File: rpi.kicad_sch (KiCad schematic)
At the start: 1 part, among them J1 Raspberry_Pi_2_3

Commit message: more schematic
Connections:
- net RO: now reaches J1.10 (GPIO15/RXD)
- net RST: now reaches J1.11 (GPIO17)
- net BI: now reaches J1.36 (GPIO16)
- net CI: now reaches J1.8 (GPIO14/TXD)
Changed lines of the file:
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@@
+    (stroke (width 0) (type default))
+  )
+  (wire (pts (xy 64.135 59.055) (xy 68.58 59.055))
     (stroke (width 0) (type default))
   )
@@
     (stroke (width 0) (type default))
   )
+  (wire (pts (xy 64.135 51.435) (xy 68.58 51.435))
+    (stroke (width 0) (type default))
+  )
+  (wire (pts (xy 64.135 48.895) (xy 68.58 48.895))
+    (stroke (width 0) (type default))
+  )
   (wire (pts (xy 86.36 104.775) (xy 86.36 106.68))
     (stroke (width 0) (type default))
@@
     (stroke (width 0) (type default))
   )
+  (wire (pts (xy 64.135 56.515) (xy 68.58 56.515))
+    (stroke (width 0) (type default))
+  )
   (global_label "GND" (shape input) (at 87.63 111.76 0) (fields_autoplaced)
     (effects (font (size 1.27 1.27)) (justify left))
@@
     (effects (font (size 1.27 1.27)) (justify left))
   )
+  (hierarchical_label "RO" (shape input) (at 64.135 51.435 180) (fields_autoplaced)
+    (effects (font (size 1.27 1.27)) (justify right))
+  )
+  (hierarchical_label "BI" (shape output) (at 64.135 56.515 180) (fields_autoplaced)
+    (effects (font (size 1.27 1.27)) (justify right))
+  )
+  (hierarchical_label "RST" (shape output) (at 64.135 59.055 180) (fields_autoplaced)
+    (effects (font (size 1.27 1.27)) (justify right))
+  )
+  (hierarchical_label "CI" (shape output) (at 64.135 48.895 180) (fields_autoplaced)
+    (effects (font (size 1.27 1.27)) (justify right))
+  )
   (hierarchical_label "5V" (shape input) (at 85.09 31.75 90) (fields_autoplaced)

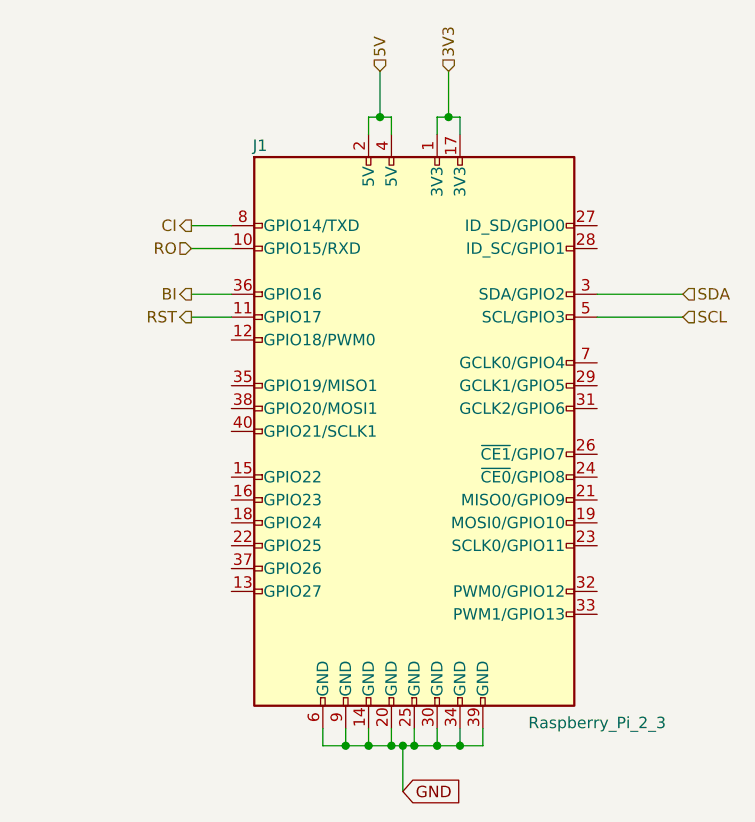
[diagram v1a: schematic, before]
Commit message: cleanup level shifters. LCRC inductor for buck
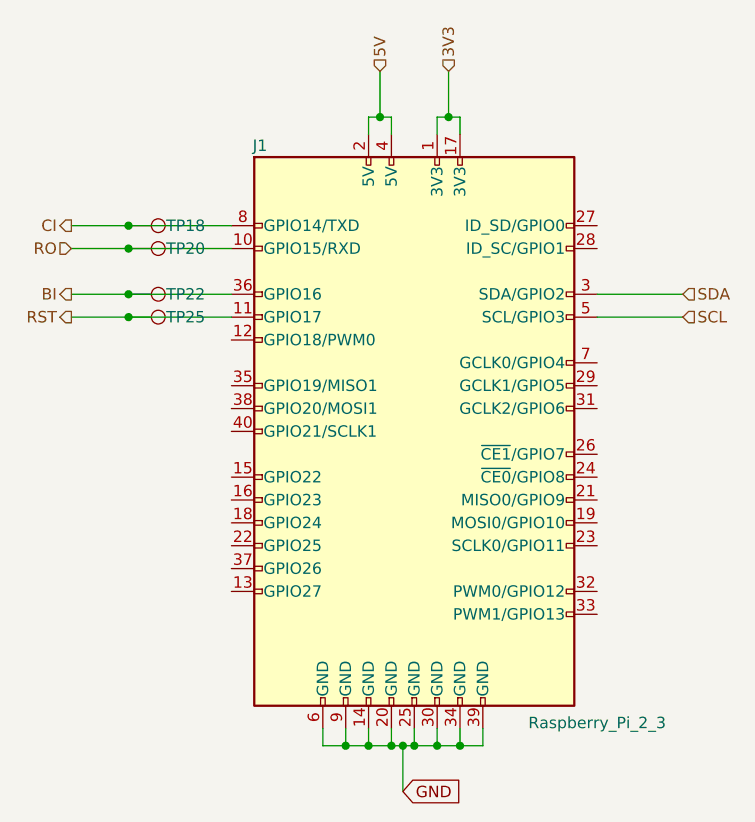
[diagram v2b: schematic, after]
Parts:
- added TP18, TP20, TP22, TP25: TestPoint, TestPoint:TestPoint_Pad_D1.5mm, symbol Connector:TestPoint
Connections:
- net BI: now also TP22.1
- net CI: now also TP18.1
- net RO: now also TP20.1
- net RST: now also TP25.1
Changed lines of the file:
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@@
   (junction (at 92.71 36.83) (diameter 0) (color 0 0 0 0)
   )
+  (junction (at 57.15 59.055) (diameter 0) (color 0 0 0 0)
+  )
+  (junction (at 57.15 51.435) (diameter 0) (color 0 0 0 0)
+  )
+  (junction (at 57.15 56.515) (diameter 0) (color 0 0 0 0)
+  )
   (junction (at 91.44 106.68) (diameter 0) (color 0 0 0 0)
   )
@@
   (junction (at 81.28 106.68) (diameter 0) (color 0 0 0 0)
   )
+  (junction (at 57.15 48.895) (diameter 0) (color 0 0 0 0)
+  )
   (junction (at 88.9 106.68) (diameter 0) (color 0 0 0 0)
   )
@@
     (stroke (width 0) (type default))
   )
-  (wire (pts (xy 64.135 59.055) (xy 68.58 59.055))
+  (wire (pts (xy 50.8 59.055) (xy 57.15 59.055))
     (stroke (width 0) (type default))
   )
@@
     (stroke (width 0) (type default))
   )
+  (wire (pts (xy 57.15 51.435) (xy 68.58 51.435))
+    (stroke (width 0) (type default))
+  )
   (wire (pts (xy 78.74 106.68) (xy 81.28 106.68))
     (stroke (width 0) (type default))
   )
+  (wire (pts (xy 57.15 56.515) (xy 68.58 56.515))
+    (stroke (width 0) (type default))
+  )
   (wire (pts (xy 83.82 36.83) (xy 85.09 36.83))
     (stroke (width 0) (type default))
@@
     (stroke (width 0) (type default))
   )
-  (wire (pts (xy 64.135 51.435) (xy 68.58 51.435))
-    (stroke (width 0) (type default))
-  )
-  (wire (pts (xy 64.135 48.895) (xy 68.58 48.895))
+  (wire (pts (xy 50.8 51.435) (xy 57.15 51.435))
+    (stroke (width 0) (type default))
+  )
+  (wire (pts (xy 50.8 48.895) (xy 57.15 48.895))
     (stroke (width 0) (type default))
   )
@@
     (stroke (width 0) (type default))
   )
+  (wire (pts (xy 57.15 59.055) (xy 68.58 59.055))
+    (stroke (width 0) (type default))
+  )
+  (wire (pts (xy 57.15 48.895) (xy 68.58 48.895))
+    (stroke (width 0) (type default))
+  )
   (wire (pts (xy 81.28 106.68) (xy 83.82 106.68))
     (stroke (width 0) (type default))
@@
     (stroke (width 0) (type default))
   )
-  (wire (pts (xy 64.135 56.515) (xy 68.58 56.515))
+  (wire (pts (xy 50.8 56.515) (xy 57.15 56.515))
     (stroke (width 0) (type default))
   )
@@
     (effects (font (size 1.27 1.27)) (justify left))
   )
-  (hierarchical_label "RO" (shape input) (at 64.135 51.435 180) (fields_autoplaced)
+  (hierarchical_label "RO" (shape input) (at 50.8 51.435 180) (fields_autoplaced)
     (effects (font (size 1.27 1.27)) (justify right))
   )
-  (hierarchical_label "BI" (shape output) (at 64.135 56.515 180) (fields_autoplaced)
+  (hierarchical_label "BI" (shape output) (at 50.8 56.515 180) (fields_autoplaced)
     (effects (font (size 1.27 1.27)) (justify right))
   )
-  (hierarchical_label "RST" (shape output) (at 64.135 59.055 180) (fields_autoplaced)
+  (hierarchical_label "RST" (shape output) (at 50.8 59.055 180) (fields_autoplaced)
     (effects (font (size 1.27 1.27)) (justify right))
   )
-  (hierarchical_label "CI" (shape output) (at 64.135 48.895 180) (fields_autoplaced)
+  (hierarchical_label "CI" (shape output) (at 50.8 48.895 180) (fields_autoplaced)
     (effects (font (size 1.27 1.27)) (justify right))
   )
@@
   (hierarchical_label "SDA" (shape input) (at 118.745 56.515 0) (fields_autoplaced)
     (effects (font (size 1.27 1.27)) (justify left))
+  )
+  (symbol (lib_id "Connector:TestPoint") (at 57.15 51.435 270) (mirror x) (unit 1)
+    (in_bom yes) (on_board yes) (dnp no)
+    (property "Reference" "TP20" (at 63.5 51.435 90)
+      (effects (font (size 1.27 1.27)))
+    )
+    (property "Value" "TestPoint" (at 62.865 50.1651 90)
+      (effects (font (size 1.27 1.27)) (justify left) hide)
+    )
+    (property "Footprint" "TestPoint:TestPoint_Pad_D1.5mm" (at 57.15 46.355 0)
+      (effects (font (size 1.27 1.27)) hide)
+    )
+    (property "Datasheet" "~" (at 57.15 46.355 0)
+      (effects (font (size 1.27 1.27)) hide)
+    )
+    (property "DNP" "T" (at 57.15 51.435 0)
+      (effects (font (size 1.27 1.27)) hide)
+    )
+    (pin "1")
+    (instances
+      (project "Hashat"
+        (path "/00740941-7ad8-466a-a267-188591e2b5c4/5aa25910-cf6c-433c-86f8-40d28be84b47"
+          (reference "TP20") (unit 1)
+        )
+        (path "/00740941-7ad8-466a-a267-188591e2b5c4/17c7154e-4e6a-44f7-b397-e76bf5123af9"
+          (reference "TP20") (unit 1)
+        )
+      )
+      (project "bitaxeMax"
+        (path "/e63e39d7-6ac0-4ffd-8aa3-1841a4541b55/4cf9c075-d009-4c35-9949-adda70ae20c7"
+          (reference "TP24") (unit 1)
+        )
+      )
+    )
+  )
+  (symbol (lib_id "Connector:TestPoint") (at 57.15 48.895 270) (mirror x) (unit 1)
+    (in_bom yes) (on_board yes) (dnp no)
+    (property "Reference" "TP18" (at 63.5 48.895 90)
+      (effects (font (size 1.27 1.27)))
+    )
+    (property "Value" "TestPoint" (at 62.865 47.6251 90)
+      (effects (font (size 1.27 1.27)) (justify left) hide)
+    )
+    (property "Footprint" "TestPoint:TestPoint_Pad_D1.5mm" (at 57.15 43.815 0)
+      (effects (font (size 1.27 1.27)) hide)
+    )
+    (property "Datasheet" "~" (at 57.15 43.815 0)
+      (effects (font (size 1.27 1.27)) hide)
+    )
+    (property "DNP" "T" (at 57.15 48.895 0)
+      (effects (font (size 1.27 1.27)) hide)
+    )
+    (pin "1")
+    (instances
+      (project "Hashat"
+        (path "/00740941-7ad8-466a-a267-188591e2b5c4/5aa25910-cf6c-433c-86f8-40d28be84b47"
+          (reference "TP18") (unit 1)
+        )
+        (path "/00740941-7ad8-466a-a267-188591e2b5c4/17c7154e-4e6a-44f7-b397-e76bf5123af9"
+          (reference "TP18") (unit 1)
+        )
+      )
+      (project "bitaxeMax"
+        (path "/e63e39d7-6ac0-4ffd-8aa3-1841a4541b55/4cf9c075-d009-4c35-9949-adda70ae20c7"
+          (reference "TP24") (unit 1)
+        )
+      )
+    )
   )
   (symbol (lib_id "Connector:Raspberry_Pi_2_3") (at 88.9 71.755 0) (unit 1)
@@
         )
       )
+    )
+  )
+  (symbol (lib_id "Connector:TestPoint") (at 57.15 56.515 270) (mirror x) (unit 1)
+    (in_bom yes) (on_board yes) (dnp no)
+    (property "Reference" "TP22" (at 63.5 56.515 90)
+      (effects (font (size 1.27 1.27)))
+    )
+    (property "Value" "TestPoint" (at 62.865 55.2451 90)
+      (effects (font (size 1.27 1.27)) (justify left) hide)
+    )
+    (property "Footprint" "TestPoint:TestPoint_Pad_D1.5mm" (at 57.15 51.435 0)
+      (effects (font (size 1.27 1.27)) hide)
+    )
+    (property "Datasheet" "~" (at 57.15 51.435 0)
+      (effects (font (size 1.27 1.27)) hide)
+    )
+    (property "DNP" "T" (at 57.15 56.515 0)
+      (effects (font (size 1.27 1.27)) hide)
+    )
+    (pin "1")
+    (instances
+      (project "Hashat"
+        (path "/00740941-7ad8-466a-a267-188591e2b5c4/5aa25910-cf6c-433c-86f8-40d28be84b47"
+          (reference "TP22") (unit 1)
+        )
+        (path "/00740941-7ad8-466a-a267-188591e2b5c4/17c7154e-4e6a-44f7-b397-e76bf5123af9"
+          (reference "TP22") (unit 1)
+        )
+      )
+      (project "bitaxeMax"
+        (path "/e63e39d7-6ac0-4ffd-8aa3-1841a4541b55/4cf9c075-d009-4c35-9949-adda70ae20c7"
+          (reference "TP24") (unit 1)
+        )
+      )
+    )
+  )
+  (symbol (lib_id "Connector:TestPoint") (at 57.15 59.055 270) (mirror x) (unit 1)
+    (in_bom yes) (on_board yes) (dnp no)
+    (property "Reference" "TP25" (at 63.5 59.055 90)
+      (effects (font (size 1.27 1.27)))
+    )
+    (property "Value" "TestPoint" (at 62.865 57.7851 90)
+      (effects (font (size 1.27 1.27)) (justify left) hide)
+    )
+    (property "Footprint" "TestPoint:TestPoint_Pad_D1.5mm" (at 57.15 53.975 0)
+      (effects (font (size 1.27 1.27)) hide)
+    )
+    (property "Datasheet" "~" (at 57.15 53.975 0)
+      (effects (font (size 1.27 1.27)) hide)
+    )
+    (property "DNP" "T" (at 57.15 59.055 0)
+      (effects (font (size 1.27 1.27)) hide)
+    )
+    (pin "1")
+    (instances
+      (project "Hashat"
+        (path "/00740941-7ad8-466a-a267-188591e2b5c4/5aa25910-cf6c-433c-86f8-40d28be84b47"
+          (reference "TP25") (unit 1)
+        )
+        (path "/00740941-7ad8-466a-a267-188591e2b5c4/17c7154e-4e6a-44f7-b397-e76bf5123af9"
+          (reference "TP25") (unit 1)
+        )
+      )
+      (project "bitaxeMax"
+        (path "/e63e39d7-6ac0-4ffd-8aa3-1841a4541b55/4cf9c075-d009-4c35-9949-adda70ae20c7"
+          (reference "TP24") (unit 1)
+        )
+      )

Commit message: fully removed BI (and pulled down at the BM1397)
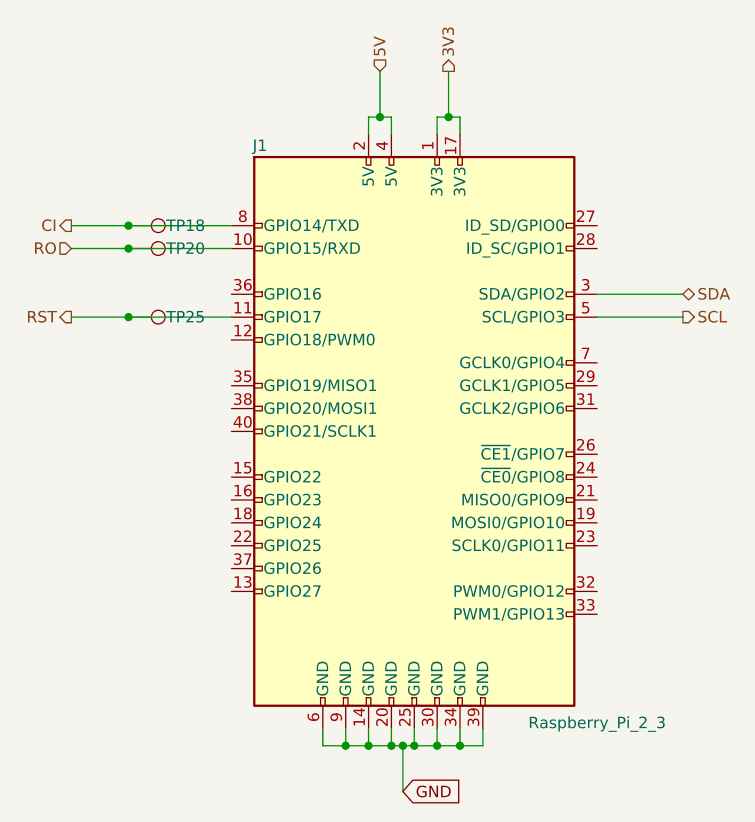
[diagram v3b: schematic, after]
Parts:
- removed TP22: TestPoint, TestPoint:TestPoint_Pad_D1.5mm, symbol Connector:TestPoint
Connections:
- net BI: no longer names the net of J1.36 (GPIO16)
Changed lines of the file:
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@@
   (junction (at 57.15 51.435) (diameter 0) (color 0 0 0 0)
   )
-  (junction (at 57.15 56.515) (diameter 0) (color 0 0 0 0)
-  )
   (junction (at 91.44 106.68) (diameter 0) (color 0 0 0 0)
   )
@@
     (stroke (width 0) (type default))
   )
-  (wire (pts (xy 57.15 56.515) (xy 68.58 56.515))
-    (stroke (width 0) (type default))
-  )
   (wire (pts (xy 83.82 36.83) (xy 85.09 36.83))
     (stroke (width 0) (type default))
@@
   )
   (wire (pts (xy 83.82 106.68) (xy 86.36 106.68))
-    (stroke (width 0) (type default))
-  )
-  (wire (pts (xy 50.8 56.515) (xy 57.15 56.515))
     (stroke (width 0) (type default))
   )
@@
     )
   )
-  (hierarchical_label "3V3" (shape input) (at 92.71 31.75 90) (fields_autoplaced)
+  (hierarchical_label "3V3" (shape output) (at 92.71 31.75 90) (fields_autoplaced)
     (effects (font (size 1.27 1.27)) (justify left))
   )
@@
     (effects (font (size 1.27 1.27)) (justify right))
   )
-  (hierarchical_label "BI" (shape output) (at 50.8 56.515 180) (fields_autoplaced)
-    (effects (font (size 1.27 1.27)) (justify right))
-  )
   (hierarchical_label "RST" (shape output) (at 50.8 59.055 180) (fields_autoplaced)
     (effects (font (size 1.27 1.27)) (justify right))
@@
     (effects (font (size 1.27 1.27)) (justify left))
   )
-  (hierarchical_label "SCL" (shape input) (at 118.745 59.055 0) (fields_autoplaced)
-    (effects (font (size 1.27 1.27)) (justify left))
-  )
-  (hierarchical_label "SDA" (shape input) (at 118.745 56.515 0) (fields_autoplaced)
+  (hierarchical_label "SCL" (shape output) (at 118.745 59.055 0) (fields_autoplaced)
+    (effects (font (size 1.27 1.27)) (justify left))
+  )
+  (hierarchical_label "SDA" (shape bidirectional) (at 118.745 56.515 0) (fields_autoplaced)
     (effects (font (size 1.27 1.27)) (justify left))
   )
@@
         )
       )
-    )
-  )
-  (symbol (lib_id "Connector:TestPoint") (at 57.15 56.515 270) (mirror x) (unit 1)
-    (in_bom yes) (on_board yes) (dnp no)
-    (property "Reference" "TP22" (at 63.5 56.515 90)
-      (effects (font (size 1.27 1.27)))
-    )
-    (property "Value" "TestPoint" (at 62.865 55.2451 90)
-      (effects (font (size 1.27 1.27)) (justify left) hide)
-    )
-    (property "Footprint" "TestPoint:TestPoint_Pad_D1.5mm" (at 57.15 51.435 0)
-      (effects (font (size 1.27 1.27)) hide)
-    )
-    (property "Datasheet" "~" (at 57.15 51.435 0)
-      (effects (font (size 1.27 1.27)) hide)
-    )
-    (property "DNP" "T" (at 57.15 56.515 0)
-      (effects (font (size 1.27 1.27)) hide)
-    )
-    (pin "1")
-    (instances
-      (project "Hashat"
-        (path "/00740941-7ad8-466a-a267-188591e2b5c4/5aa25910-cf6c-433c-86f8-40d28be84b47"
-          (reference "TP22") (unit 1)
-        )
-        (path "/00740941-7ad8-466a-a267-188591e2b5c4/17c7154e-4e6a-44f7-b397-e76bf5123af9"
-          (reference "TP22") (unit 1)
-        )
-      )
-      (project "bitaxeMax"
-        (path "/e63e39d7-6ac0-4ffd-8aa3-1841a4541b55/4cf9c075-d009-4c35-9949-adda70ae20c7"
-          (reference "TP24") (unit 1)
-        )
-      )

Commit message: added initial BOM
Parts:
- TP18, TP20, TP25: now left out of the parts list
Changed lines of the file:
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@@
   )
   (symbol (lib_id "Connector:TestPoint") (at 57.15 51.435 270) (mirror x) (unit 1)
-    (in_bom yes) (on_board yes) (dnp no)
+    (in_bom no) (on_board yes) (dnp no)
     (property "Reference" "TP20" (at 63.5 51.435 90)
       (effects (font (size 1.27 1.27)))
@@
   )
   (symbol (lib_id "Connector:TestPoint") (at 57.15 48.895 270) (mirror x) (unit 1)
-    (in_bom yes) (on_board yes) (dnp no)
+    (in_bom no) (on_board yes) (dnp no)
     (property "Reference" "TP18" (at 63.5 48.895 90)
       (effects (font (size 1.27 1.27)))
@@
   )
   (symbol (lib_id "Connector:TestPoint") (at 57.15 59.055 270) (mirror x) (unit 1)
-    (in_bom yes) (on_board yes) (dnp no)
+    (in_bom no) (on_board yes) (dnp no)
     (property "Reference" "TP25" (at 63.5 59.055 90)
       (effects (font (size 1.27 1.27)))
